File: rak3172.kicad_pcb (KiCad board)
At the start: 4 copper layers, 40 x 30 mm, 82 parts, among them Q1 AO3401, Q2 SI2302, SW1 SW_Push, SW2 SW_Push, U1 AP6683, U2 RAK3172-SiP, U3 TP733xx, U4 UHE4913, U5 QMC6308, U6 L80RE-M37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

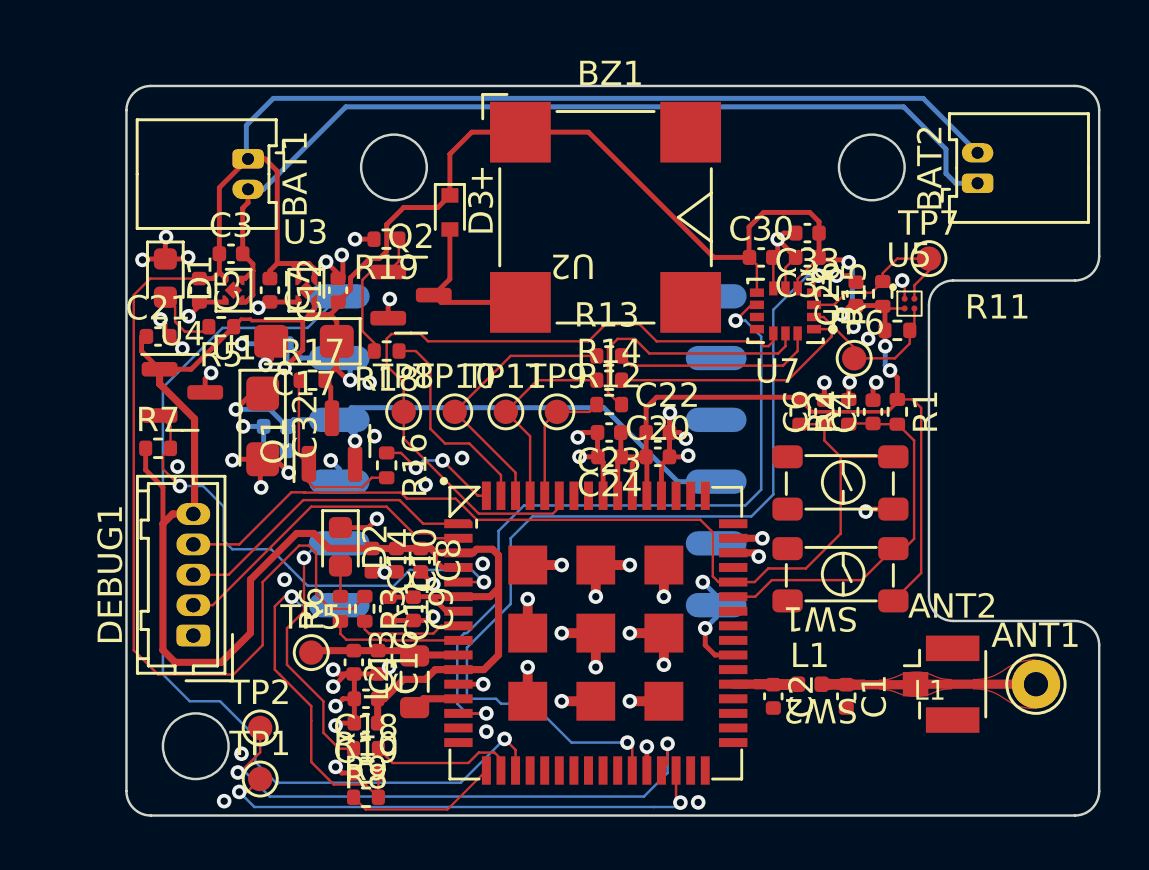
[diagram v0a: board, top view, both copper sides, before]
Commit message: Q, ANT, D name deleted
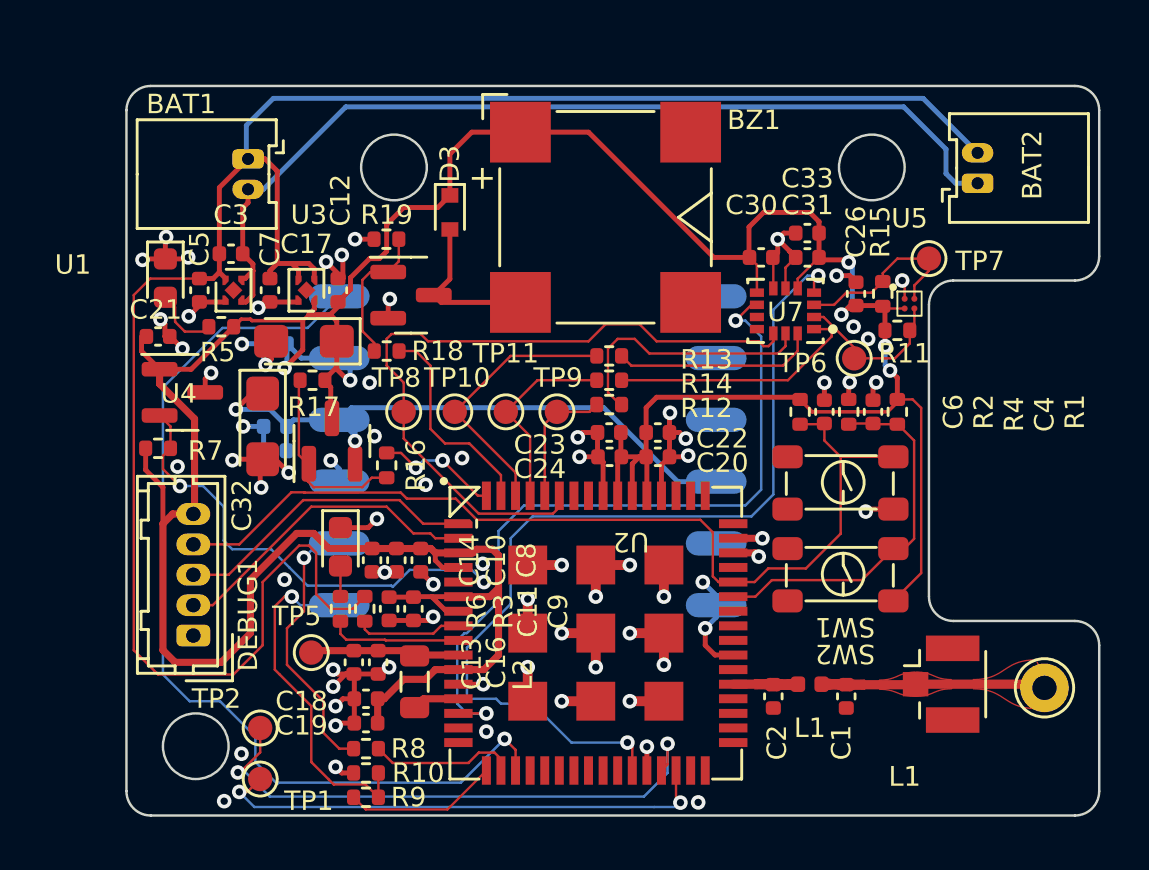
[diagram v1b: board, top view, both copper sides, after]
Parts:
- moved ANT1 0.38 mm to (217.8, 109.8)
